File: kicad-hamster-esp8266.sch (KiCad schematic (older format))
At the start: 33 parts

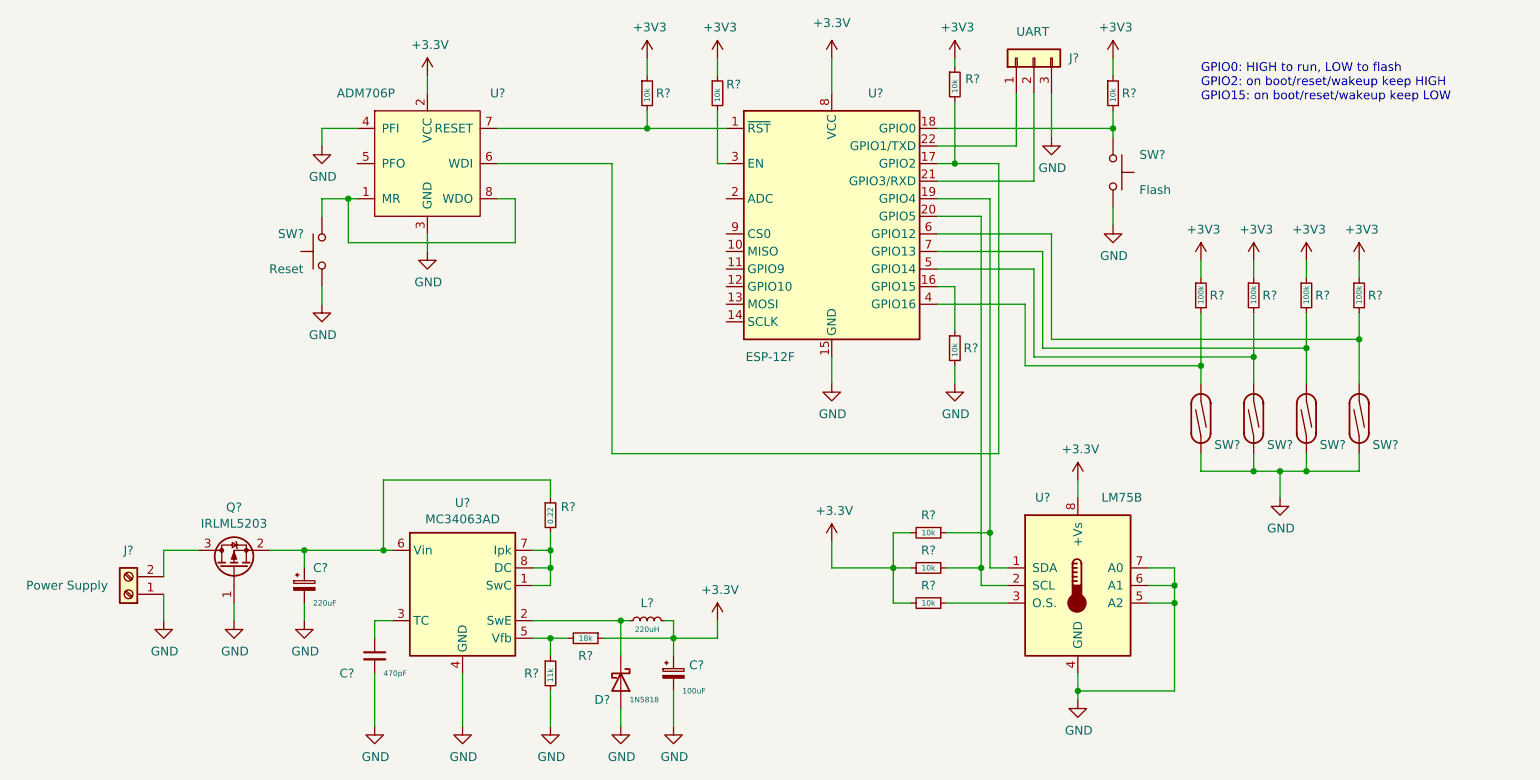
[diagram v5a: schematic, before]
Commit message: ADC: add photoresistor circuitry
Signed-off-by: Sergey Matyukevich <geomatsi@gmail.com>
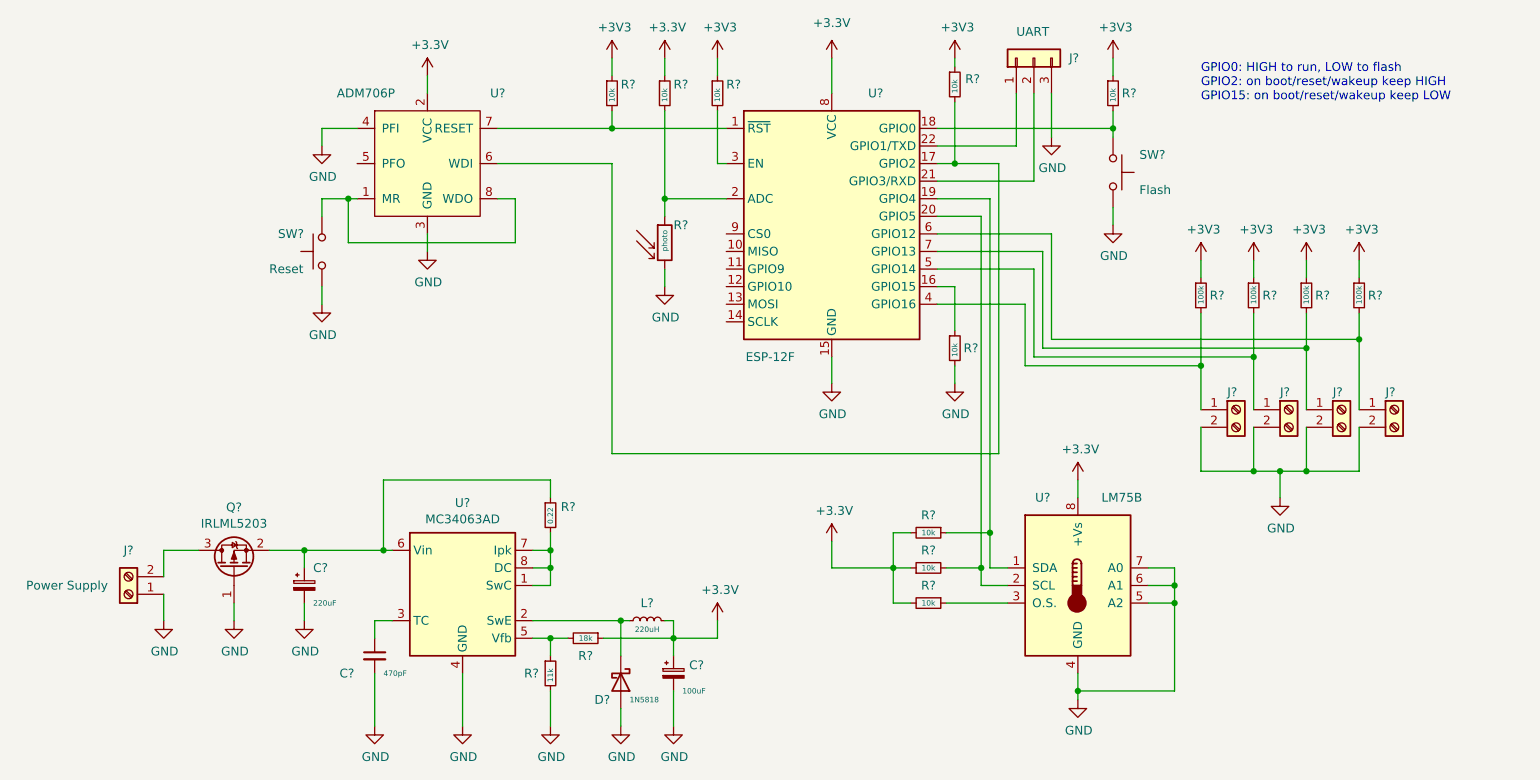
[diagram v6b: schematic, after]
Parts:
- removed SW? (x4): SW_Reed, symbol Switch:SW_Reed
- added J? (x4): Screw_Terminal_01x02, symbol Connector:Screw_Terminal_01x02
- added R?: 10k, symbol Device:R_Small
- added R?: photo, symbol Device:R_PHOTO
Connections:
- net +3V3: now also R?.1
- net GND: now also J?.2 (Pin_2), J?.2 (Pin_2), J?.2 (Pin_2), J?.2 (Pin_2), R?.2
- net at U?.2 (ADC): now also R?.1, R?.2
- net at R?.2, U?.4 (GPIO16): now also J?.1 (Pin_1)
- net at R?.2, U?.5 (GPIO14): now also J?.1 (Pin_1)
- net at R?.2, U?.6 (GPIO12): now also J?.1 (Pin_1)
- net at R?.2, U?.7 (GPIO13): now also J?.1 (Pin_1)
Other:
- moved on the sheet: R?
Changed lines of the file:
@@
 L Device:R_Small R?
 U 1 1 5F0D8CB8
-P 4450 2500
-F 0 "R?" H 4500 2500 50  0000 L CNN
-F 1 "10k" V 4450 2450 31  0000 L CNN
-F 2 "" H 4450 2500 50  0001 C CNN
-F 3 "~" H 4450 2500 50  0001 C CNN
-	1    4450 2500
+P 4250 2500
+F 0 "R?" H 4300 2550 50  0000 L CNN
+F 1 "10k" V 4250 2450 31  0000 L CNN
+F 2 "" H 4250 2500 50  0001 C CNN
+F 3 "~" H 4250 2500 50  0001 C CNN
+	1    4250 2500
 	1    0    0    -1
 $EndComp
@@
 L power:+3V3 #PWR?
 U 1 1 5F0F95D4
-P 4450 2300
-F 0 "#PWR?" H 4450 2150 50  0001 C CNN
-F 1 "+3V3" H 4465 2475 50  0000 C CNN
-F 2 "" H 4450 2300 50  0001 C CNN
-F 3 "" H 4450 2300 50  0001 C CNN
-	1    4450 2300
+P 4250 2300
+F 0 "#PWR?" H 4250 2150 50  0001 C CNN
+F 1 "+3V3" H 4265 2475 50  0000 C CNN
+F 2 "" H 4250 2300 50  0001 C CNN
+F 3 "" H 4250 2300 50  0001 C CNN
+	1    4250 2300
 	1    0    0    -1
 $EndComp
@@
 	7100 2400 7100 2300
 Wire Wire Line
-	4450 2400 4450 2300
+	4250 2400 4250 2300
 $Comp
 L power:GND #PWR?
@@
 $EndComp
 Wire Wire Line
-	7600 4050 7600 4150
-Wire Wire Line
 	6600 4050 7600 4050
 Wire Wire Line
@@
 Wire Wire Line
 	6750 3900 8500 3900
-Wire Wire Line
-	7600 4550 7600 4650
 Wire Wire Line
 	7600 4650 7900 4650
@@
 	7900 3450 7900 3550
 Wire Wire Line
-	8500 4150 8500 3900
-Wire Wire Line
-	8200 4150 8200 3950
-Wire Wire Line
-	7900 4150 7900 4000
-Wire Wire Line
-	8500 4650 8500 4550
-Wire Wire Line
 	8200 4650 8500 4650
-Wire Wire Line
-	8200 4650 8200 4550
-Wire Wire Line
-	7900 4550 7900 4650
 $Comp
 L Device:R_Small R?
@@
 	1    7900 3450
 	1    0    0    -1
-$EndComp
-$Comp
-L Switch:SW_Reed SW?
-U 1 1 5F0BCC12
-P 7600 4350
-F 0 "SW?" V 7450 4200 50  0000 C CNN
-F 1 "SW_Reed" H 7600 4482 50  0001 C CNN
-F 2 "" H 7600 4350 50  0001 C CNN
-F 3 "~" H 7600 4350 50  0001 C CNN
-	1    7600 4350
-	0    -1   -1   0
-$EndComp
-$Comp
-L Switch:SW_Reed SW?
-U 1 1 5F0BC4C3
-P 7900 4350
-F 0 "SW?" V 7750 4200 50  0000 C CNN
-F 1 "SW_Reed" H 7900 4482 50  0001 C CNN
-F 2 "" H 7900 4350 50  0001 C CNN
-F 3 "~" H 7900 4350 50  0001 C CNN
-	1    7900 4350
-	0    -1   -1   0
-$EndComp
-$Comp
-L Switch:SW_Reed SW?
-U 1 1 5F0BBD95
-P 8200 4350
-F 0 "SW?" V 8050 4200 50  0000 C CNN
-F 1 "SW_Reed" H 8200 4482 50  0001 C CNN
-F 2 "" H 8200 4350 50  0001 C CNN
-F 3 "~" H 8200 4350 50  0001 C CNN
-	1    8200 4350
-	0    -1   -1   0
-$EndComp
-$Comp
-L Switch:SW_Reed SW?
-U 1 1 5F0BB0DF
-P 8500 4350
-F 0 "SW?" V 8350 4200 50  0000 C CNN
-F 1 "SW_Reed" H 8500 4482 50  0001 C CNN
-F 2 "" H 8500 4350 50  0001 C CNN
-F 3 "~" H 8500 4350 50  0001 C CNN
-	1    8500 4350
-	0    -1   -1   0
 $EndComp
 $Comp
@@
 $EndComp
 Wire Wire Line
-	3600 2700 4450 2700
-Wire Wire Line
-	4450 2600 4450 2700
-Connection ~ 4450 2700
-Wire Wire Line
-	4450 2700 4900 2700
+	3600 2700 4250 2700
+Wire Wire Line
+	4250 2600 4250 2700
+Connection ~ 4250 2700
+Wire Wire Line
+	4250 2700 4900 2700
 $Comp
 L power:+3.3V #PWR?
@@
 	6450 2900 6200 2900
 Connection ~ 6200 2900
+$Comp
+L power:+3.3V #PWR?
+U 1 1 5F15AB4B
+P 4550 2300
+F 0 "#PWR?" H 4550 2150 50  0001 C CNN
+F 1 "+3.3V" H 4565 2475 50  0000 C CNN
+F 2 "" H 4550 2300 50  0001 C CNN
+F 3 "" H 4550 2300 50  0001 C CNN
+	1    4550 2300
+	1    0    0    -1
+$EndComp
+$Comp
+L Device:R_Small R?
+U 1 1 5F15BB16
+P 4550 2500
+F 0 "R?" H 4600 2550 50  0000 L CNN
+F 1 "10k" V 4550 2450 31  0000 L CNN
+F 2 "" H 4550 2500 50  0001 C CNN
+F 3 "~" H 4550 2500 50  0001 C CNN
+	1    4550 2500
+	1    0    0    -1
+$EndComp
+$Comp
+L Device:R_PHOTO R?
+U 1 1 5F15C60E
+P 4550 3350
+F 0 "R?" H 4600 3450 50  0000 L CNN
+F 1 "photo" V 4550 3300 31  0000 L CNN
+F 2 "" V 4600 3100 50  0001 L CNN
+F 3 "~" H 4550 3300 50  0001 C CNN
+	1    4550 3350
+	1    0    0    -1
+$EndComp
+$Comp
+L power:GND #PWR?
+U 1 1 5F15CF8C
+P 4550 3600
+F 0 "#PWR?" H 4550 3350 50  0001 C CNN
+F 1 "GND" H 4555 3425 50  0000 C CNN
+F 2 "" H 4550 3600 50  0001 C CNN
+F 3 "" H 4550 3600 50  0001 C CNN
+	1    4550 3600
+	1    0    0    -1
+$EndComp
+Wire Wire Line
+	4550 2300 4550 2400
+Wire Wire Line
+	4550 2600 4550 3100
+Wire Wire Line
+	4550 3500 4550 3600
+Wire Wire Line
+	4900 3100 4550 3100
+Connection ~ 4550 3100
+Wire Wire Line
+	4550 3100 4550 3200
+$Comp
+L Connector:Screw_Terminal_01x02 J?
+U 1 1 5F1A7DB1
+P 8700 4300
+F 0 "J?" H 8650 4400 50  0000 L CNN
+F 1 "Screw_Terminal_01x02" H 8780 4200 50  0001 L CNN
+F 2 "" H 8700 4300 50  0001 C CNN
+F 3 "~" H 8700 4300 50  0001 C CNN
+	1    8700 4300
+	1    0    0    -1
+$EndComp
+$Comp
+L Connector:Screw_Terminal_01x02 J?
+U 1 1 5F1A9503
+P 8400 4300
+F 0 "J?" H 8350 4400 50  0000 L CNN
+F 1 "Screw_Terminal_01x02" H 8480 4200 50  0001 L CNN
+F 2 "" H 8400 4300 50  0001 C CNN
+F 3 "~" H 8400 4300 50  0001 C CNN
+	1    8400 4300
+	1    0    0    -1
+$EndComp
+$Comp
+L Connector:Screw_Terminal_01x02 J?
+U 1 1 5F1AE8E4
+P 8100 4300
+F 0 "J?" H 8050 4400 50  0000 L CNN
+F 1 "Screw_Terminal_01x02" H 8180 4200 50  0001 L CNN
+F 2 "" H 8100 4300 50  0001 C CNN
+F 3 "~" H 8100 4300 50  0001 C CNN
+	1    8100 4300
+	1    0    0    -1
+$EndComp
+$Comp
+L Connector:Screw_Terminal_01x02 J?
+U 1 1 5F1AF1CC
+P 7800 4300
+F 0 "J?" H 7750 4400 50  0000 L CNN
+F 1 "Screw_Terminal_01x02" H 7880 4200 50  0001 L CNN
+F 2 "" H 7800 4300 50  0001 C CNN
+F 3 "~" H 7800 4300 50  0001 C CNN
+	1    7800 4300
+	1    0    0    -1
+$EndComp
+Wire Wire Line
+	7600 4050 7600 4300
+Wire Wire Line
+	7600 4400 7600 4650
+Wire Wire Line
+	7900 4400 7900 4650
+Wire Wire Line
+	7900 4000 7900 4300
+Wire Wire Line
+	8200 4400 8200 4650
+Wire Wire Line
+	8200 3950 8200 4300
+Wire Wire Line
+	8500 4400 8500 4650
+Wire Wire Line
+	8500 3900 8500 4300
 $EndSCHEMATC

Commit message: pcb: net list and preliminary placement
Signed-off-by: Sergey Matyukevich <geomatsi@gmail.com>
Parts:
- C1, C3: renamed from C?; footprint (none) -> Capacitor_THT:CP_Radial_D8.0mm_P3.80mm
- C2: renamed from C?; footprint (none) -> Capacitor_SMD:C_1206_3216Metric_Pad1.42x1.75mm_HandSolder
- J1, J3, J4, J5, J6: renamed from J?; footprint (none) -> TerminalBlock_Phoenix:TerminalBlock_Phoenix_PT-1,5-2-3.5-H_1x02_P3.50mm_Horizontal
- J2: renamed from J?; footprint (none) -> Connector_PinHeader_2.54mm:PinHeader_1x03_P2.54mm_Vertical
- L1: renamed from L?; footprint (none) -> Inductor_THT:L_Radial_D7.2mm_P3.00mm_MuRATA_1700
- R1, R10, R11, R12, R13, R14, R15, R16, R17, R2, R3, R4, R5, R7, R8, R9: renamed from R?; footprint (none) -> Resistor_SMD:R_1206_3216Metric_Pad1.42x1.75mm_HandSolder
- R6: renamed from R?; footprint (none) -> Capacitor_THT:CP_Radial_D8.0mm_P3.80mm
- SW1: renamed from SW?; footprint (none) -> Button_Switch_SMD:SW_SPST_REED_CT05-XXXX-J1
- SW2: renamed from SW?; footprint (none) -> Connector_PinHeader_2.54mm:PinHeader_1x02_P2.54mm_Vertical
- gave numbers to parts that had none: 6

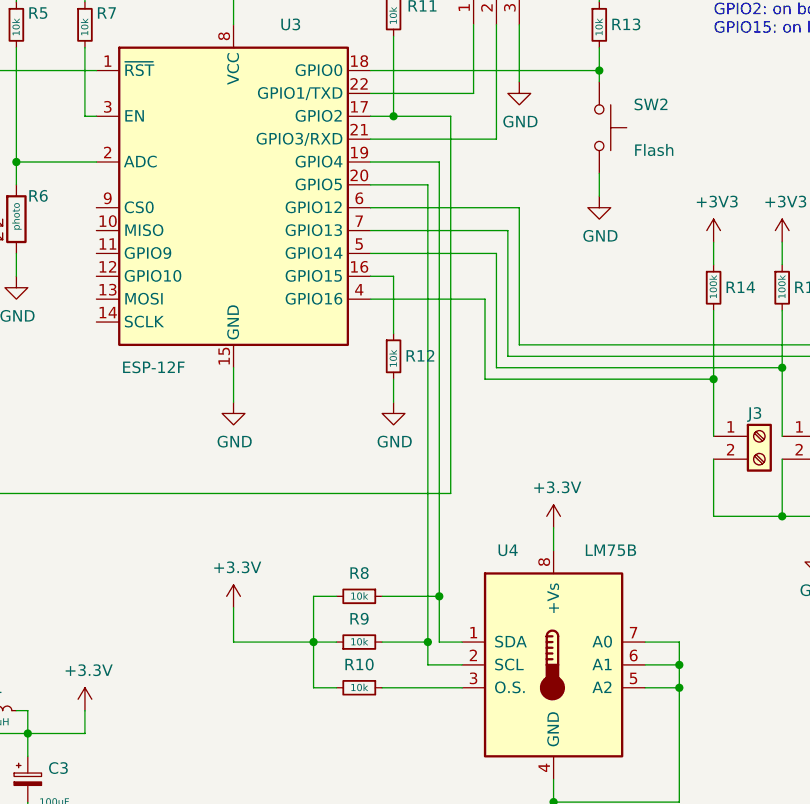
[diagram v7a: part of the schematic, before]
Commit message: pcb: first layout version
Signed-off-by: Sergey Matyukevich <geomatsi@gmail.com>
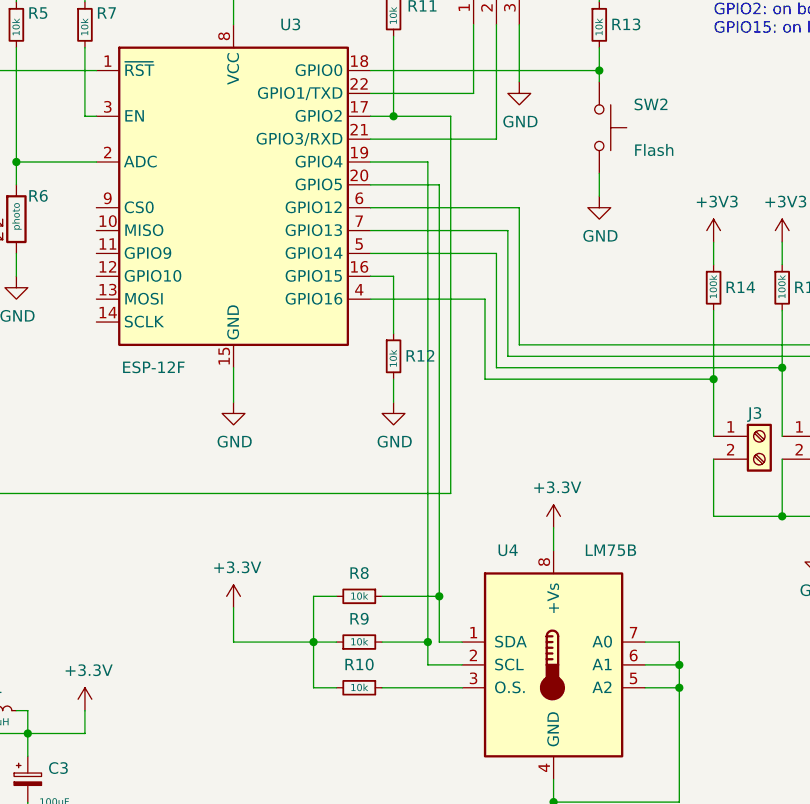
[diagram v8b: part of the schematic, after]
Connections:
- net at R8.1, U4.1 (SDA): now also U3.20 (GPIO5); no longer U3.19 (GPIO4)
- net at R9.2, U4.2 (SCL): now also U3.19 (GPIO4); no longer U3.20 (GPIO5)
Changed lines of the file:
@@
 $EndComp
-Wire Wire Line
-	6100 3100 6400 3100
-Wire Wire Line
-	6400 3100 6400 5000
 Wire Wire Line
 	6400 5200 6500 5200
@@
 Wire Wire Line
 	6350 5300 6350 5200
-Wire Wire Line
-	6350 3200 6100 3200
 $Comp
 L power:GND #PWR0125
@@
 Wire Wire Line
 	6150 5000 6400 5000
-Connection ~ 6400 5000
 Wire Wire Line
 	6400 5000 6400 5200
 Wire Wire Line
 	6150 5200 6350 5200
-Connection ~ 6350 5200
-Wire Wire Line
-	6350 5200 6350 3200
 Wire Wire Line
 	5500 5050 5500 5200
@@
 Wire Wire Line
 	8500 3900 8500 4300
+Wire Wire Line
+	6100 3100 6350 3100
+Connection ~ 6350 5200
+Wire Wire Line
+	6350 3100 6350 5200
+Wire Wire Line
+	6100 3200 6400 3200
+Wire Wire Line
+	6400 3200 6400 5000
+Connection ~ 6400 5000
 $EndSCHEMATC
